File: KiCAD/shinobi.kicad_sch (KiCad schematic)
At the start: 111 parts, among them IC1 TPS62825DMQT, IC2 TPS62825DMQT, IC3 74LVC2G17GW-Q100H, J2 61300711121, J3 61301011121, J4 61300211121, J5 USB_C_Receptacle_USB2.0_16P, Q1 UMH3N, U1 TV5725, U2 W9864G2JH-6, U5 SI5351A, U6 CH343P, U7 ESP8285, Y1 CRYSTAL2.5X2.0, Y2 CRYSTAL2.5X2.0, Y3 26MHz

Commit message: shinobi2 routing
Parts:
- removed C29: C-USC0402, Capacitor_SMD:C_0402_1005Metric, symbol Device:C
- added C66: C_Feedthrough, SamacSys_Parts:NFM18PC106D0J3L, symbol Device:C_Feedthrough
- Y1, Y2, Y3: footprint Crystal:Crystal_SMD_2520-4Pin_2.5x2.0mm -> SamacSys_Parts:Crystal_SMD_2520-4Pin_2.5x2.0mm
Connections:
- net +2V5: now also R1.1, RN3.5 (R4.2), RN3.6 (R3.2), C66.3; no longer U1.157 (DAVD)
- net B: now also R7.1, R8.2
- net CHIP_EN: now also RN3.4 (R4.1); no longer RN2.8 (R1.2)
- net G: now also R5.1, R6.2
- net GND: now also R2.2, R4.1, R6.1, R8.1, U1.122 (PAVS), U1.126 (PVSS9), U1.136 (PVSS10), U1.143 (VSS3), U1.148 (PVSS11), U1.153 (DVSS), U1.156 (DAVS), C66.2, C66.4
- net GPIO2: now also RN2.8 (R1.2); no longer RN2.6 (R3.2)
- net R: now also R3.1, R4.2
- net RST: now also RN3.3 (R3.1); no longer RN2.5 (R4.2)
- net SCL: now also RN2.5 (R4.2)
- net SDA: now also RN2.6 (R3.2)
- net at R3.2: now also C3.1
- net at U1.75 (RSTN): now also R1.2
- net at R5.2: now also C4.1
- net at C5.1: now also R7.2
- new net: C66.1, U1.157 (DAVD)
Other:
- moved on the sheet: C14, C15, C16, C18, C19, C21, C22, C30, C40, C42, R1

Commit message: Update PCB and BOM
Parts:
- AE1: value Antenna -> AMCA72-2R470G-S1F-T4
- C18: renamed from C63; value 0.1μF -> 130pF
- C19: renamed from C62; value 0.1μF -> 130pF
- C20: renamed from C17; value C_Feedthrough -> NFM18PC106D0J3L
- C22: renamed from C1; value C-USC0402 -> 0.1μF
- C24: renamed from C56; value 0.1μF -> 47pF
- C25: renamed from C57; value 0.1μF -> 47pF
- C26: renamed from C58; value 0.1μF -> 47pF
- C27: renamed from C59; value 0.1μF -> 15pF
- C28: renamed from C60; value 0.1μF -> 15pF
- C29: renamed from C61; value 0.1μF -> 15pF
- C30: renamed from C2; value C-USC0402 -> 0.1μF
- C31: renamed from C21; value C-USC0402 -> 0.1μF
- C32: renamed from C22; value C-USC0402 -> 0.1μF
- C36: renamed from C7; value C-USC0402 -> 47nF
- C37: renamed from C66; value C_Feedthrough -> NFM18PC106D0J3L
- C38: renamed from C8; value C-USC0402 -> 47nF
- C39: renamed from C9; value C-USC0402 -> 47nF
- C40: renamed from C14; value C-USC0402 -> 0.1μF
- C41: renamed from C15; value C-USC0402 -> 0.1μF
- C42: renamed from C3; value C-USC0402 -> 47nF
- C43: renamed from C6; value C-USC0402 -> 1nF
- C44: renamed from C16; value C-USC0402 -> 0.1μF
- C45: renamed from C20; value C-USC0402 -> 0.1μF
- C46: renamed from C4; value C-USC0402 -> 47nF
- C47: renamed from C23; value C-USC0402 -> 0.1μF
- C48: renamed from C24; value C-USC0402 -> 0.1μF
- C49: renamed from C5; value C-USC0402 -> 47nF
- C50: renamed from C25; value C-USC0402 -> 0.1μF
- C51: renamed from C26; value C-USC0402 -> 0.1μF
- C52: renamed from C10; value C-USC0402 -> 15pF
- C53: renamed from C27; value C-USC0402 -> 0.1μF
- C54: renamed from C11; value C-USC0402 -> 15pF
- C55: renamed from C28; value C-USC0402 -> 0.1μF
- C56: renamed from C30; value C-USC0402 -> 0.1μF
- C57: renamed from C42; value C-USC0402 -> 0.1μF
- C58: renamed from C43; value C-USC0402 -> 0.1μF
- C59: renamed from C44; value C-USC0402 -> 0.1μF
- C60: renamed from C45; value C-USC0402 -> 0.1μF
- C61: renamed from C46; value C-USC0402 -> 0.1μF
- C62: renamed from C47; value C-USC0402 -> 0.1μF
- C63: renamed from C48; value C-USC0402 -> 0.1μF
- C64: renamed from C49; value C-USC0402 -> 0.1μF
- C65: renamed from C50; value C-USC0402 -> 0.1μF
- FB1: renamed from FB3; value FerriteBead_Small -> BLM15BD221SN1D; footprint (none) -> Inductor_SMD:L_0402_1005Metric
- FB2: value FerriteBead_Small -> BLM15BD221SN1D; footprint (none) -> Inductor_SMD:L_0402_1005Metric
- FB3: renamed from FB1; value FerriteBead_Small -> BLM15BD221SN1D; footprint (none) -> Inductor_SMD:L_0402_1005Metric
- J2: renamed from J5; value USB_C_Receptacle_USB2.0_16P -> 217179-0001
- J4: renamed from J2; footprint shinobi:61300711121 -> shinobi:61300711121_11687645
- Q1: value UMH3N -> PUMH13-QF
- R10: renamed from R17; value R_Small -> 75Ω
- R11: renamed from R18; value R_Small -> 75Ω
- R12: renamed from R2; value R_Small -> 150Ω
- R13: renamed from R10; value R_Small -> 3kΩ
- R14: renamed from R9; value R_Small -> 75Ω
- R15: renamed from R3; value R_Small -> 200Ω
- R16: renamed from R4; value R_Small -> 75Ω
- R17: renamed from R5; value R_Small -> 200Ω
- R18: renamed from R6; value R_Small -> 75Ω
- R19: renamed from R7; value R_Small -> 200Ω
- R20: renamed from R8; value R_Small -> 75Ω
- R21: renamed from R1; value R_Small -> 4.7kΩ
- R22: renamed from R11; value R_Small -> 1MΩ
- R3: renamed from R13; value 12k -> 316kΩ
- R4: renamed from R19; value 12k -> 100kΩ
- R5: renamed from R22; value 12k -> 150kΩ
- R6: renamed from R23; value 12k -> 100kΩ
- R7: renamed from R15; value 12k -> 33Ω
- R8: renamed from R14; value 12k -> 33Ω
- R9: renamed from R16; value R_Small -> 75Ω
- RN1: renamed from RN2; value R_Pack04 -> EXB-28V123JX
- RN2: renamed from RN3; value R_Pack04 -> EXB-28V123JX
- U1: renamed from IC2; value TPS62825DMQT -> TPS62825DMQR; Mouser Part Number 595-TPS62825DMQT -> TPS62825DMQR
- U2: renamed from IC1; value TPS62825DMQT -> TPS62825DMQR; Mouser Part Number 595-TPS62825DMQT -> TPS62825DMQR
- Y1: renamed from Y3; value 26MHz -> ECS-260-7-36B-CKY-TR
- Y2: value CRYSTAL2.5X2.0 -> ECS-250-10-36B2-CTN-TR
- Y3: renamed from Y1; value CRYSTAL2.5X2.0 -> 830108208409
- renumbered C37 to C1, C31 to C10, C55 to C11, C35 to C12, C32 to C13, C64 to C14, C34 to C15, C13 to C16, C33 to C17, C65 to C2, C51 to C21, C53 to C23, C36 to C3, C18 to C33, C19 to C34, C40 to C35, C52 to C4, C12 to C5, C38 to C6, C39 to C7, C41 to C8, C54 to C9, J4 to J1, R20 to R1, R21 to R2, U6 to U3, U7 to U4, IC3 to U5, U5 to U6, U1 to U7, U2 to U8
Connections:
- net at C54.2, U7.124 (XTIN), Y3.3 (2): now also R22.2
- net at C52.2, U7.125 (XTOUT), Y3.1: now also R22.1
- no-connect marks 21 -> 61
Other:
- note added: "ESP8285"
- note added: "Regulators"
- note added: "USB-C to Serial"
- note removed: "U1"
- moved on the sheet: C1, C10, C11, C13, C14, C2, C20, C6, C7, C8, C9, L1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

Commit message: wip
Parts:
- C16, C17: value 10pF -> 15pF
- C6, C7: value 120pF -> 130pF
- Y1: value ECS-260-7-36B-CKY-TR -> 26MHz 10pF 2520
- Y2: value ECS-250-10-36B2-CTN-TR -> 25MHz 10pF 2520
- Y3: value 830108208409 -> 27MHz 10pF 2520

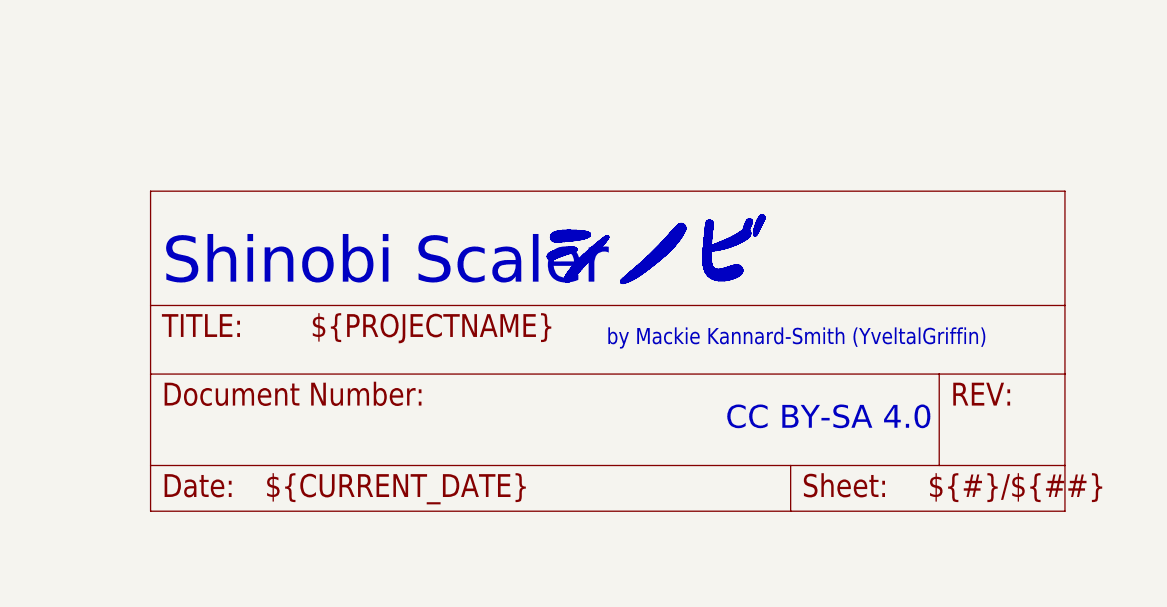
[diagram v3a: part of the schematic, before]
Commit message: embed fonts, layout tweaks
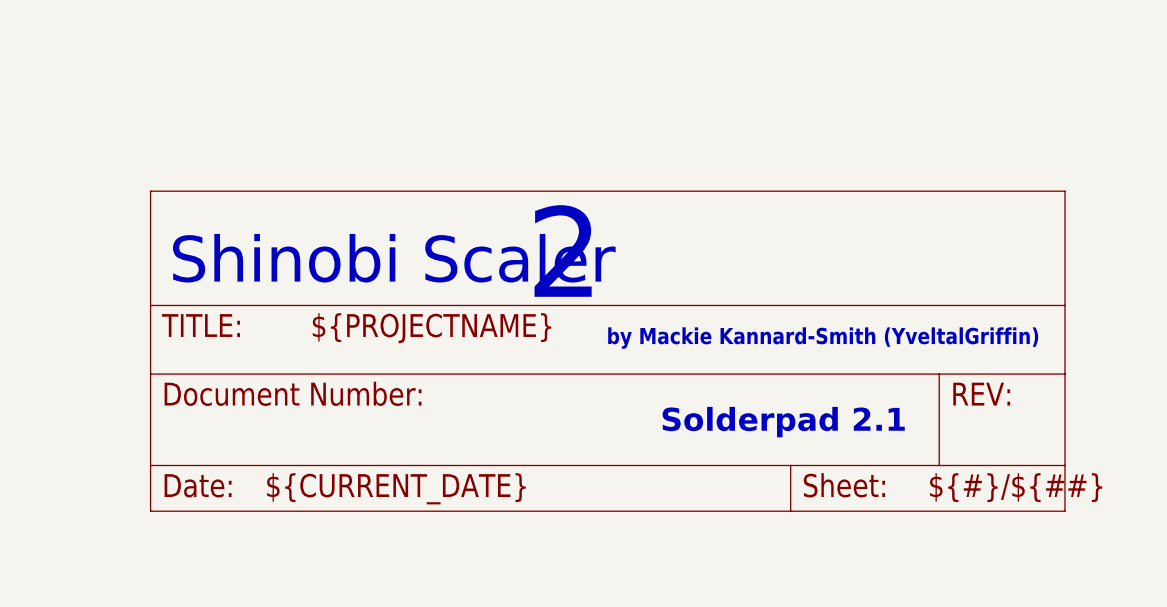
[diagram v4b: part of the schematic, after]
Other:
- note added: "2"
- note added: "Solderpad 2.1"
- note removed: "CC BY-SA 4.0"

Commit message: small updates
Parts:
- removed C13: 10μF, Capacitor_SMD:C_0603_1608Metric, symbol Device:C_Small
- added C13, C66: 100uF, Capacitor_Tantalum_SMD:CP_EIA-2012-12_Kemet-R, symbol Device:C_Polarized_Small
- added D1: LED, LED_SMD:LED_0603_1608Metric, symbol Device:LED
- added R23: 1kΩ, Resistor_SMD:R_0402_1005Metric, symbol Device:R_Small
- added SW1: SW_Push, Button_Switch_SMD:SW_SPST_B3U-1000P, symbol Switch:SW_Push
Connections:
- net +2V5: now also C13.1, C66.1; no longer U4.5 (VDD_RTC)
- net GND: now also C13.2, C66.2, D1.1 (K), SW1.2
- net VBUS: now also R23.1
- net at U4.9 (GPIO14): now also SW1.1
- new net: D1.2 (A), R23.2
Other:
- note added: "Place an additional 316k in parallel with R4 to set Vout = 3.1V"
- moved on the sheet: C20

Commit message: updating files
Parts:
- C23: renamed from C22; symbol Device:C -> Device:C_Small
- C31: renamed from C30; symbol Device:C -> Device:C_Small
- C32: renamed from C31; symbol Device:C -> Device:C_Small
- C33: renamed from C32; symbol Device:C -> Device:C_Small
- C37: renamed from C36; symbol Device:C -> Device:C_Small
- C39: renamed from C38; symbol Device:C -> Device:C_Small
- C40: renamed from C39; symbol Device:C -> Device:C_Small
- C41: renamed from C40; symbol Device:C -> Device:C_Small
- C42: renamed from C41; symbol Device:C -> Device:C_Small
- C43: renamed from C42; symbol Device:C -> Device:C_Small
- C44: renamed from C43; symbol Device:C -> Device:C_Small
- C45: renamed from C44; symbol Device:C -> Device:C_Small
- C46: renamed from C45; symbol Device:C -> Device:C_Small
- C47: renamed from C46; symbol Device:C -> Device:C_Small
- C48: renamed from C47; symbol Device:C -> Device:C_Small
- C49: renamed from C48; symbol Device:C -> Device:C_Small
- C50: renamed from C49; symbol Device:C -> Device:C_Small
- C51: renamed from C50; symbol Device:C -> Device:C_Small
- C52: renamed from C51; symbol Device:C -> Device:C_Small
- C53: renamed from C52; symbol Device:C -> Device:C_Small
- C54: renamed from C53; symbol Device:C -> Device:C_Small
- C55: renamed from C54; symbol Device:C -> Device:C_Small
- C56: renamed from C55; symbol Device:C -> Device:C_Small
- C57: renamed from C56; symbol Device:C -> Device:C_Small
- C58: renamed from C57; symbol Device:C -> Device:C_Small
- C59: renamed from C58; symbol Device:C -> Device:C_Small
- C60: renamed from C59; symbol Device:C -> Device:C_Small
- C61: renamed from C60; symbol Device:C -> Device:C_Small
- C62: renamed from C61; symbol Device:C -> Device:C_Small
- C63: renamed from C62; symbol Device:C -> Device:C_Small
- C64: renamed from C63; symbol Device:C -> Device:C_Small
- C65: renamed from C64; symbol Device:C -> Device:C_Small
- C66: renamed from C65; symbol Device:C -> Device:C_Small
- D1: value LED -> green
- SW1: value SW_Push -> B3U-1000P
- renumbered C14 to C13, C13 to C14, C66 to C20, C20 to C22, C23 to C24, C24 to C25, C25 to C26, C26 to C27, C27 to C28, C28 to C29, C29 to C30, C33 to C34, C34 to C35, C35 to C36, C37 to C38, R23 to R1, R9 to R10, R10 to R11, R11 to R12, R12 to R13, R13 to R14, R14 to R15, R15 to R16, R16 to R17, R17 to R18, R18 to R19, R1 to R2, R19 to R20, R20 to R21, R21 to R22, R22 to R23, R2 to R3, R3 to R4, R4 to R5, R5 to R6, R6 to R7, R7 to R8, R8 to R9
